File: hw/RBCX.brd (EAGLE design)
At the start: 100 x 100 mm, 463 parts, among them IC1 AMS1117-3.3, IC10 INA180A4, IC11 INA180A4, IC12 MPU-6050, IC13 STM32F103VCT6, IC2 DRV8833PWP, IC3 INA180A4, IC4 INA180A4, IC5 DRV8833PWP, IC6 INA180A4, IC7 INA180A4, IC8 INA180A4, IC9 INA180A4, P1 M1, P2 M2, P3 M3, P4 M4, Q1 NCE20P45Q, Q10 2N7002, Q2 NCE20P45Q, Q3 2N7002, Q4 2N7002, Q5 2N7002, Q6 2N7002, Q7 2N7002, Q8 2N7002, Q9 2N7002, X1 POWER_IN, X2 POWER_OUT, X3 52559-3092, X4 uUSB, Y1 5032/2P, Y2 3215_2P

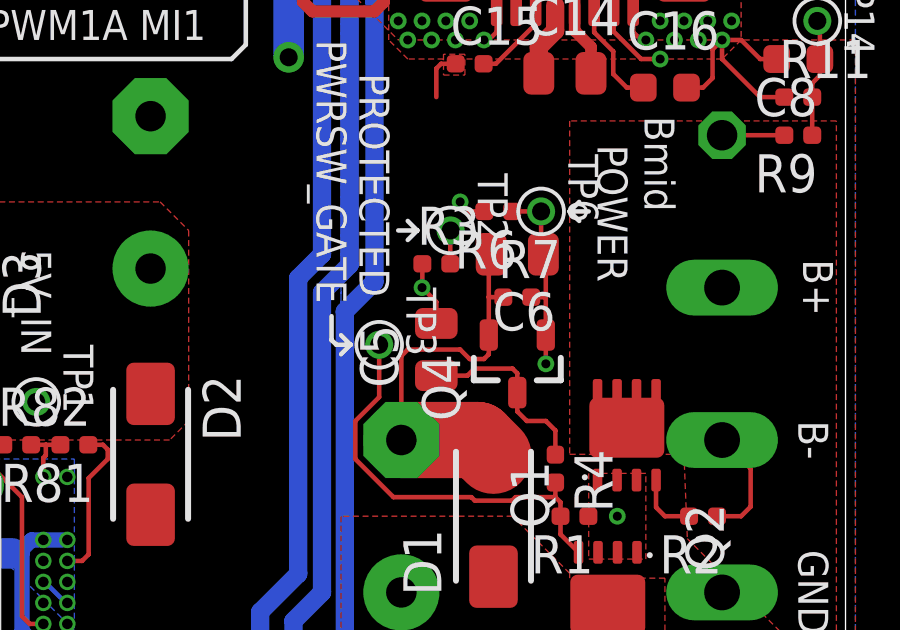
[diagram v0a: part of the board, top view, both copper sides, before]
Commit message: hw: fix power circuit capacitors value
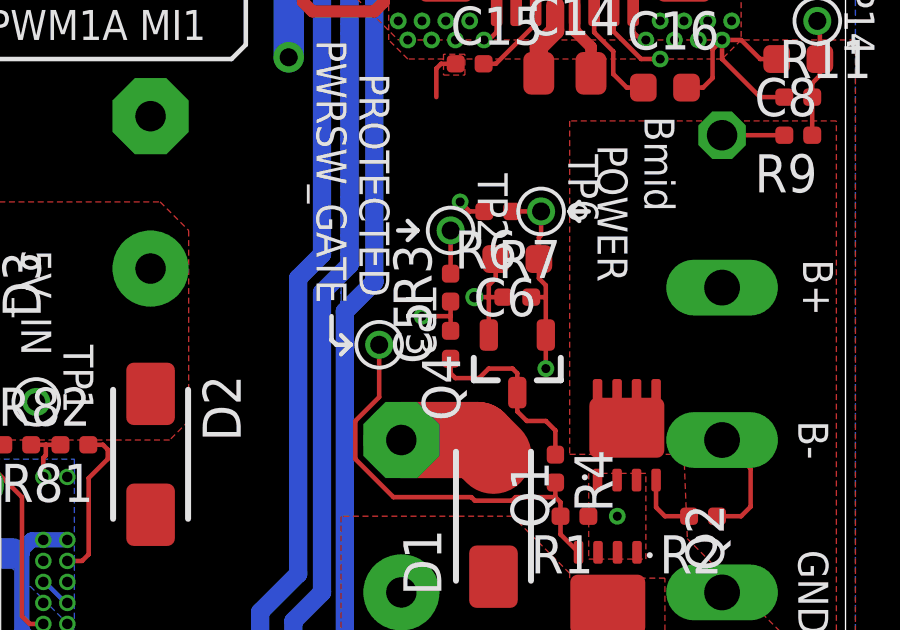
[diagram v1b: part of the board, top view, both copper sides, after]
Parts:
- C5: value 10u -> 100n; device rcl_upravena:C0805 -> rcl_upravena:C0402
- C6: value 10u -> 2u2; device rcl_upravena:C0805 -> rcl_upravena:C0603
- moved R3 0.93 mm to (86.8, 57.8), turned to 90 degrees
- moved C5 0.50 mm to (86.8, 55.9)
- moved C6 0.16 mm to (89.1, 58.7)
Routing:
- net GND: track 636.3 -> 630.1 mm, vias 141 -> 142
- net BUTTON-ON: track 157.5 -> 156.8 mm

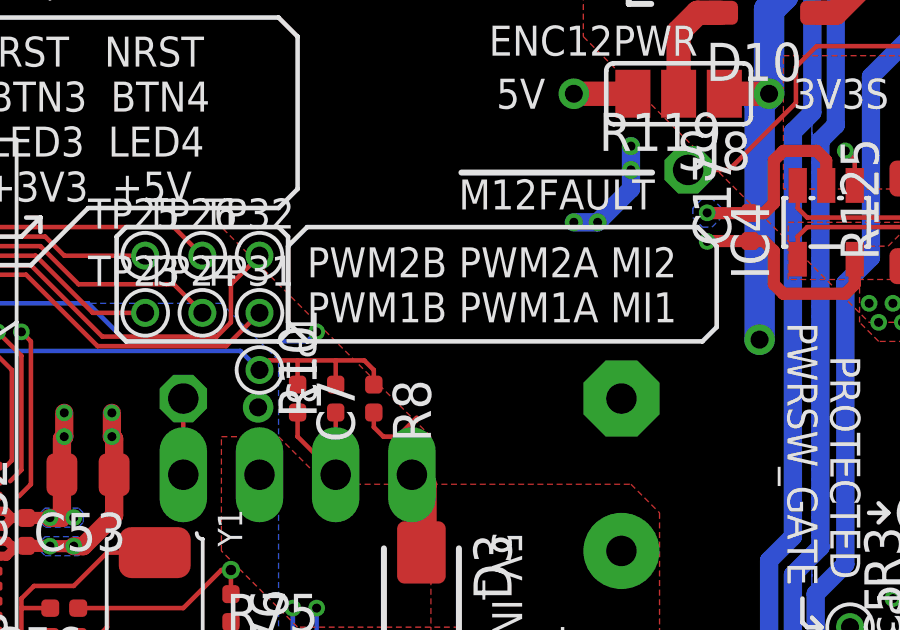
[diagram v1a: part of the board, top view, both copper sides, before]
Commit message: hw: fix power button function without battery connected (only in schematic)
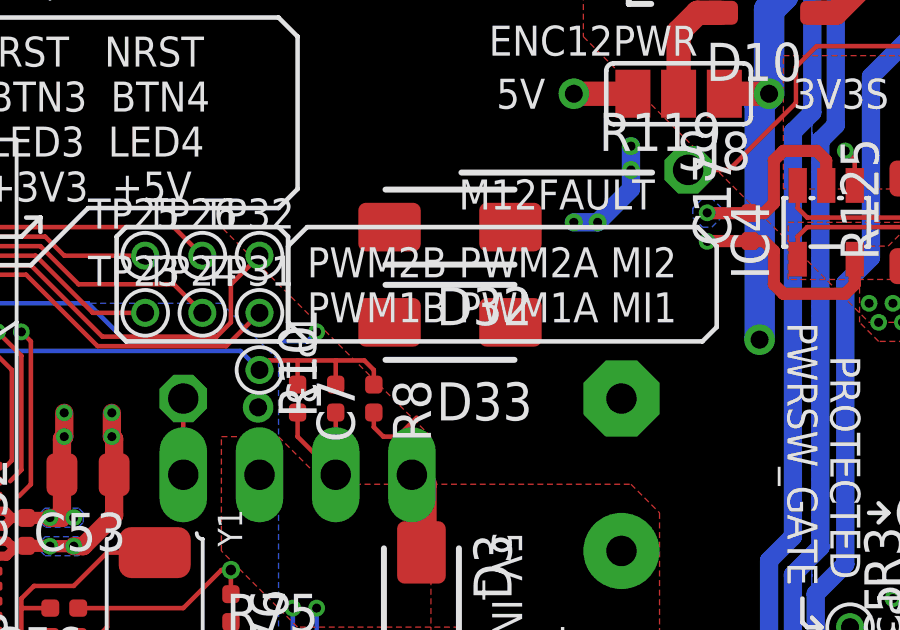
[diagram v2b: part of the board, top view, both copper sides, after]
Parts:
- added D32, D33: SS34, diode:SMA
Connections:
- net +5V: now also D32.A
- net BAT+_PROTECTED: now also D32.C, D33.C
- net VUSB: now also D33.A
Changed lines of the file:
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@@
 <attribute name="VOLTAGE" value="16V" x="89.05875" y="58.7375" size="1.778" layer="27" rot="R180" display="off"/>
 </element>
+<element name="D32" library="diode" package="SMA" value="SS34" x="71.12" y="69.215" smashed="yes" rot="R180">
+<attribute name="NAME" x="73.87" y="67.215" size="1.27" layer="25" ratio="10" rot="R180"/>
+<attribute name="VALUE" x="73.87" y="72.715" size="1.27" layer="27" ratio="10" rot="R180"/>
+</element>
+<element name="D33" library="diode" package="SMA" value="SS34" x="71.12" y="66.04" smashed="yes" rot="R180">
+<attribute name="NAME" x="73.87" y="64.04" size="1.27" layer="25" ratio="10" rot="R180"/>
+<attribute name="VALUE" x="73.87" y="69.54" size="1.27" layer="27" ratio="10" rot="R180"/>
+</element>
 </elements>
 <signals>
@@
 <wire x1="92.3925" y1="54.13375" x2="86.83625" y2="59.69" width="0.6096" layer="2"/>
 <wire x1="86.83625" y1="58.25" x2="86.83625" y2="59.69" width="0.1524" layer="1"/>
+<contactref element="D32" pad="C"/>
+<contactref element="D33" pad="C"/>
 <wire x1="92.385" y1="51.36875" x2="91.735" y2="51.36875" width="0" layer="19" extent="1-1"/>
 <wire x1="93.035" y1="51.36875" x2="92.385" y2="51.36875" width="0" layer="19" extent="1-1"/>
@@
 <wire x1="91.75" y1="48.96125" x2="92.4" y2="48.96125" width="0" layer="19" extent="1-1"/>
 <wire x1="93.05" y1="48.96125" x2="92.4" y2="48.96125" width="0" layer="19" extent="1-1"/>
+<wire x1="73.135" y1="69.215" x2="91.75" y2="48.96125" width="0" layer="19" extent="1-1"/>
+<wire x1="73.135" y1="66.04" x2="73.135" y2="69.215" width="0" layer="19" extent="1-1"/>
 </signal>
 <signal name="BAT+">
@@
 <wire x1="33.655" y1="6.604" x2="33.655" y2="6.59375" width="0.1524" layer="1"/>
 <wire x1="8.9535" y1="10.16" x2="8.96375" y2="10.16" width="0.1524" layer="1"/>
+<contactref element="D32" pad="A"/>
+<wire x1="76.835" y1="95.885" x2="76.835" y2="98.425" width="0" layer="19" extent="1-1"/>
+<wire x1="76.835" y1="93.345" x2="76.835" y2="95.885" width="0" layer="19" extent="1-1"/>
+<wire x1="76.835" y1="90.805" x2="76.835" y2="93.345" width="0" layer="19" extent="1-1"/>
+<wire x1="76.835" y1="86.36" x2="77.355" y2="87.78875" width="0" layer="19" extent="1-1"/>
+<wire x1="67.6275" y1="83.02625" x2="76.835" y2="86.36" width="0" layer="19" extent="1-1"/>
+<wire x1="66.04" y1="83.02625" x2="67.6275" y2="83.02625" width="0" layer="19" extent="1-1"/>
+<wire x1="66.04" y1="81.43875" x2="66.04" y2="83.02625" width="0" layer="19" extent="1-1"/>
+<wire x1="67.6275" y1="81.43875" x2="67.6275" y2="83.02625" width="0" layer="19" extent="1-1"/>
+<wire x1="64.325" y1="82.2325" x2="66.04" y2="83.02625" width="0" layer="19" extent="1-1"/>
+<wire x1="75.2475" y1="73.66" x2="67.6275" y2="81.43875" width="0" layer="19" extent="1-1"/>
+<wire x1="69.85" y1="60.96" x2="75.2475" y2="73.66" width="0" layer="19" extent="1-1"/>
+<wire x1="65.515" y1="33.3375" x2="70.1675" y2="58.37125" width="0" layer="19" extent="1-1"/>
+<wire x1="81.5975" y1="29.845" x2="69.5325" y2="30.7975" width="0" layer="19" extent="1-1"/>
+<wire x1="81.915" y1="8.89" x2="81.661" y2="27.94" width="0" layer="19" extent="1-1"/>
+<wire x1="81.915" y1="6.35" x2="81.915" y2="8.89" width="0" layer="19" extent="1-1"/>
+<wire x1="81.915" y1="3.81" x2="81.915" y2="6.35" width="0" layer="19" extent="1-1"/>
+<wire x1="81.915" y1="1.27" x2="81.915" y2="3.81" width="0" layer="19" extent="1-1"/>
+<wire x1="53.975" y1="8.255" x2="69.5325" y2="30.7975" width="0" layer="19" extent="1-1"/>
+<wire x1="33.655" y1="8.09625" x2="53.975" y2="8.255" width="0" layer="19" extent="1-1"/>
+<wire x1="8.9535" y1="6.35" x2="33.655" y2="6.604" width="0" layer="19" extent="1-1"/>
+<wire x1="69.105" y1="69.215" x2="8.9535" y2="2.54" width="0" layer="19" extent="1-1"/>
+<wire x1="13.335" y1="27.01" x2="8.96375" y2="10.16" width="0" layer="19" extent="1-1"/>
+<wire x1="9.36625" y1="72.39" x2="8.5725" y2="40.64" width="0" layer="19" extent="1-1"/>
+<wire x1="9.36625" y1="74.93" x2="9.36625" y2="72.39" width="0" layer="19" extent="1-1"/>
+<wire x1="17.78" y1="90.17" x2="9.36625" y2="74.93" width="0" layer="19" extent="1-1"/>
+<wire x1="17.78" y1="91.7575" x2="17.78" y2="90.17" width="0" layer="19" extent="1-1"/>
+<wire x1="19.3675" y1="91.7575" x2="17.78" y2="91.7575" width="0" layer="19" extent="1-1"/>
+<wire x1="19.3675" y1="90.17" x2="17.78" y2="90.17" width="0" layer="19" extent="1-1"/>
+<wire x1="18.9225" y1="93.6625" x2="19.3675" y2="91.7575" width="0" layer="19" extent="1-1"/>
+<wire x1="28.8925" y1="73.18375" x2="19.3675" y2="90.17" width="0" layer="19" extent="1-1"/>
 </signal>
 <signal name="ISERVO">
@@
 <wire x1="73.26" y1="45.875" x2="74.06" y2="45.875" width="0.508" layer="2"/>
 <wire x1="74.06" y1="45.875" x2="74.37375" y2="45.56125" width="0.508" layer="2"/>
+<contactref element="D33" pad="A"/>
+<wire x1="69.105" y1="66.04" x2="3.3625" y2="51.835" width="0" layer="19" extent="1-16"/>
 </signal>
 <signal name="USB_ID">

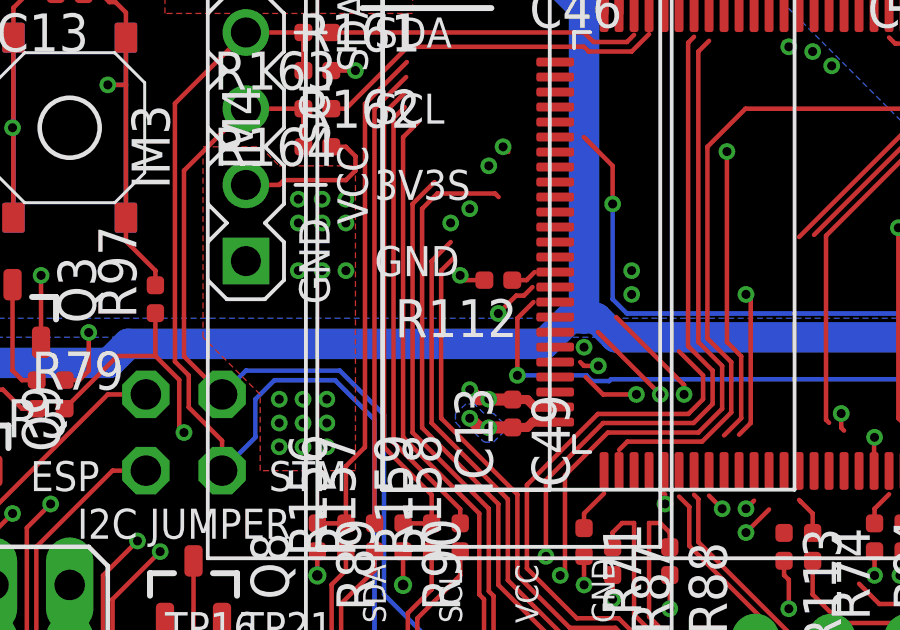
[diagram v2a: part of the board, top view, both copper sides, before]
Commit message: hw: remove resistor between STM and ESP enable
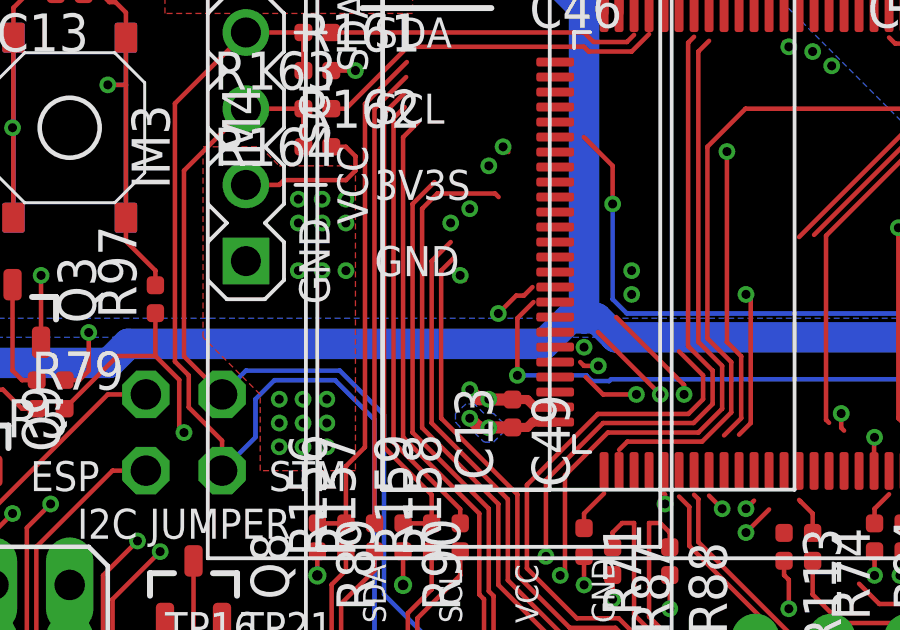
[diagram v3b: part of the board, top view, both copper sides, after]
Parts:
- removed R112: 330R, rcl_upravena:R0402
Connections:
- removed net ESP-EN: IM9.2, JP44.5, R112.2, S13.C, S13.D, S7.C, S7.D, TP60.P$1, X3.15
- net ESP_EN: now also IM9.2, JP44.5, S13.C, S13.D, S7.C, S7.D, TP60.P$1, X3.15; no longer R112.1
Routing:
- net ESP-EN: track 138.8 -> 0.00 mm, vias 4 -> 0
- net ESP_EN: track 0.86 -> 138.2 mm, vias 0 -> 4
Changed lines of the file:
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@@
 <attribute name="VALUE" x="0.47625" y="93.345" size="1.27" layer="28" rot="MR180"/>
 </element>
-<element name="R112" library="rcl_upravena" package="R0402" value="330R" x="38.4175" y="53.975" smashed="yes" rot="R180">
-<attribute name="NAME" x="39.0525" y="53.34" size="1.27" layer="25" rot="R180"/>
-<attribute name="VALUE" x="39.0525" y="55.88" size="1.27" layer="27" rot="R180"/>
-</element>
 <element name="IC12" library="MPU-6050" package="QFN50P400X400X95-24N" value="MPU-6050" x="51.435" y="24.765" smashed="yes" rot="R270">
 <attribute name="AVAILABILITY" value="Unavailable" x="51.435" y="24.765" size="1.778" layer="27" rot="R270" display="off"/>
@@
 <wire x1="4.7625" y1="38.25875" x2="6.50875" y2="38.25875" width="0.1524" layer="2"/>
 </signal>
-<signal name="ESP-EN">
-<contactref element="X3" pad="15"/>
-<contactref element="R112" pad="2"/>
-<contactref element="JP44" pad="5"/>
-<contactref element="IM9" pad="2"/>
-<contactref element="S7" pad="C"/>
-<contactref element="S7" pad="D"/>
-<contactref element="TP60" pad="P$1"/>
-<wire x1="6.16125" y1="8.90625" x2="6.16125" y2="14.90625" width="0.1524" layer="1"/>
-<wire x1="37.1475" y1="54.13375" x2="37.30625" y2="53.975" width="0.1524" layer="1"/>
-<wire x1="37.9525" y1="53.975" x2="37.30625" y2="53.975" width="0.1524" layer="1"/>
-<via x="37.1475" y="54.13375" extent="1-16" drill="0.3"/>
-<via x="9.2075" y="56.99125" extent="1-16" drill="0.3"/>
-<wire x1="9.2075" y1="56.99125" x2="8.89" y2="56.67375" width="0.1524" layer="1"/>
-<wire x1="8.89" y1="56.67375" x2="8.89" y2="44.45" width="0.1524" layer="1"/>
-<wire x1="5.715" y1="44.45" x2="8.89" y2="44.45" width="0.1524" layer="1"/>
-<wire x1="11.43" y1="38.1" x2="11.4276" y2="38.1024" width="0.1524" layer="1"/>
-<wire x1="11.4276" y1="38.1024" x2="11.4276" y2="39.6320375" width="0.1524" layer="1"/>
-<wire x1="8.89" y1="42.1696375" x2="8.89" y2="44.45" width="0.1524" layer="1"/>
-<wire x1="11.4276" y1="39.6320375" x2="8.89" y2="42.1696375" width="0.1524" layer="1"/>
-<wire x1="9.2075" y1="56.99125" x2="9.2075" y2="62.5475" width="0.1524" layer="1"/>
-<wire x1="7.9375" y1="89.05875" x2="6.82625" y2="90.17" width="0.1524" layer="1"/>
-<wire x1="9.2075" y1="56.99125" x2="27.14625" y2="56.99125" width="0.1524" layer="2"/>
-<wire x1="27.14625" y1="56.99125" x2="28.41625" y2="55.72125" width="0.1524" layer="2"/>
-<wire x1="28.41625" y1="55.72125" x2="30.63875" y2="55.72125" width="0.1524" layer="2"/>
-<wire x1="36.35375" y1="54.9275" x2="37.1475" y2="54.13375" width="0.1524" layer="2"/>
-<wire x1="36.35375" y1="54.9275" x2="31.4325" y2="54.9275" width="0.1524" layer="2"/>
-<wire x1="31.4325" y1="54.9275" x2="30.63875" y2="55.72125" width="0.1524" layer="2"/>
-<wire x1="3.3625" y1="44.835" x2="4.3775" y2="44.835" width="0.1524" layer="16"/>
-<wire x1="4.445" y1="44.7675" x2="4.3775" y2="44.835" width="0.1524" layer="16"/>
-<wire x1="4.445" y1="44.7675" x2="4.7625" y2="44.7675" width="0.1524" layer="16"/>
-<via x="4.7625" y="44.7675" extent="1-16" drill="0.3"/>
-<wire x1="4.7625" y1="44.7675" x2="5.3975" y2="44.7675" width="0.1524" layer="1"/>
-<wire x1="5.3975" y1="44.7675" x2="5.715" y2="44.45" width="0.1524" layer="1"/>
-<wire x1="9.2075" y1="62.5475" x2="10.795" y2="64.135" width="0.1524" layer="1"/>
-<wire x1="10.795" y1="64.135" x2="10.795" y2="88.265" width="0.1524" layer="1"/>
-<wire x1="10.00125" y1="89.05875" x2="7.9375" y2="89.05875" width="0.1524" layer="1"/>
-<wire x1="10.795" y1="88.265" x2="10.00125" y2="89.05875" width="0.1524" layer="1"/>
-<wire x1="9.36625" y1="92.71" x2="6.82625" y2="90.17" width="0.1524" layer="2"/>
-<wire x1="7.77875" y1="39.0525" x2="7.18185" y2="38.4556" width="0.1524" layer="2"/>
-<wire x1="10.4775" y1="39.0525" x2="11.43" y2="38.1" width="0.1524" layer="2"/>
-<wire x1="7.77875" y1="39.0525" x2="10.4775" y2="39.0525" width="0.1524" layer="2"/>
-<wire x1="7.18185" y1="16.70685" x2="6.985" y2="16.51" width="0.1524" layer="2"/>
-<via x="6.985" y="16.51" extent="1-16" drill="0.3"/>
-<wire x1="6.985" y1="16.51" x2="6.16125" y2="15.68625" width="0.1524" layer="1"/>
-<wire x1="6.16125" y1="15.68625" x2="6.16125" y2="14.90625" width="0.1524" layer="1"/>
-<wire x1="7.18185" y1="38.4556" x2="7.18185" y2="16.70685" width="0.1524" layer="2"/>
-<contactref element="S13" pad="C"/>
-<contactref element="S13" pad="D"/>
-<wire x1="6.16125" y1="8.90625" x2="6.16125" y2="14.90625" width="0.1524" layer="16"/>
-<wire x1="6.16125" y1="14.90625" x2="6.16125" y2="15.68625" width="0.1524" layer="16"/>
-<wire x1="6.16125" y1="15.68625" x2="6.985" y2="16.51" width="0.1524" layer="16"/>
-</signal>
 <signal name="PWRSW_GATE">
 <contactref element="R1" pad="2"/>
@@
 </signal>
 <signal name="ESP_EN">
-<contactref element="R112" pad="1"/>
-<wire x1="38.8825" y1="53.975" x2="39.35875" y2="53.975" width="0.1524" layer="1"/>
-<wire x1="39.62875" y1="54.245" x2="39.35875" y2="53.975" width="0.1524" layer="1"/>
 <contactref element="IC13" pad="85"/>
-<wire x1="46.4425" y1="47.615" x2="39.62875" y2="54.245" width="0" layer="19" extent="1-1"/>
+<contactref element="X3" pad="15"/>
+<contactref element="JP44" pad="5"/>
+<contactref element="IM9" pad="2"/>
+<contactref element="S7" pad="C"/>
+<contactref element="S7" pad="D"/>
+<contactref element="TP60" pad="P$1"/>
+<wire x1="6.16125" y1="8.90625" x2="6.16125" y2="14.90625" width="0.1524" layer="1"/>
+<wire x1="37.1475" y1="54.13375" x2="37.30625" y2="53.975" width="0.1524" layer="1"/>
+<via x="37.1475" y="54.13375" extent="1-16" drill="0.3"/>
+<via x="9.2075" y="56.99125" extent="1-16" drill="0.3"/>
+<wire x1="9.2075" y1="56.99125" x2="8.89" y2="56.67375" width="0.1524" layer="1"/>
+<wire x1="8.89" y1="56.67375" x2="8.89" y2="44.45" width="0.1524" layer="1"/>
+<wire x1="5.715" y1="44.45" x2="8.89" y2="44.45" width="0.1524" layer="1"/>
+<wire x1="11.43" y1="38.1" x2="11.4276" y2="38.1024" width="0.1524" layer="1"/>
+<wire x1="11.4276" y1="38.1024" x2="11.4276" y2="39.6320375" width="0.1524" layer="1"/>
+<wire x1="8.89" y1="42.1696375" x2="8.89" y2="44.45" width="0.1524" layer="1"/>
+<wire x1="11.4276" y1="39.6320375" x2="8.89" y2="42.1696375" width="0.1524" layer="1"/>
+<wire x1="9.2075" y1="56.99125" x2="9.2075" y2="62.5475" width="0.1524" layer="1"/>
+<wire x1="7.9375" y1="89.05875" x2="6.82625" y2="90.17" width="0.1524" layer="1"/>
+<wire x1="9.2075" y1="56.99125" x2="27.14625" y2="56.99125" width="0.1524" layer="2"/>
+<wire x1="27.14625" y1="56.99125" x2="28.41625" y2="55.72125" width="0.1524" layer="2"/>
+<wire x1="28.41625" y1="55.72125" x2="30.63875" y2="55.72125" width="0.1524" layer="2"/>
+<wire x1="36.35375" y1="54.9275" x2="37.1475" y2="54.13375" width="0.1524" layer="2"/>
+<wire x1="36.35375" y1="54.9275" x2="31.4325" y2="54.9275" width="0.1524" layer="2"/>
+<wire x1="31.4325" y1="54.9275" x2="30.63875" y2="55.72125" width="0.1524" layer="2"/>
+<wire x1="3.3625" y1="44.835" x2="4.3775" y2="44.835" width="0.1524" layer="16"/>
+<wire x1="4.445" y1="44.7675" x2="4.3775" y2="44.835" width="0.1524" layer="16"/>
+<wire x1="4.445" y1="44.7675" x2="4.7625" y2="44.7675" width="0.1524" layer="16"/>
+<via x="4.7625" y="44.7675" extent="1-16" drill="0.3"/>
+<wire x1="4.7625" y1="44.7675" x2="5.3975" y2="44.7675" width="0.1524" layer="1"/>
+<wire x1="5.3975" y1="44.7675" x2="5.715" y2="44.45" width="0.1524" layer="1"/>
+<wire x1="9.2075" y1="62.5475" x2="10.795" y2="64.135" width="0.1524" layer="1"/>
+<wire x1="10.795" y1="64.135" x2="10.795" y2="88.265" width="0.1524" layer="1"/>
+<wire x1="10.00125" y1="89.05875" x2="7.9375" y2="89.05875" width="0.1524" layer="1"/>
+<wire x1="10.795" y1="88.265" x2="10.00125" y2="89.05875" width="0.1524" layer="1"/>
+<wire x1="9.36625" y1="92.71" x2="6.82625" y2="90.17" width="0.1524" layer="2"/>
+<wire x1="7.77875" y1="39.0525" x2="7.18185" y2="38.4556" width="0.1524" layer="2"/>
+<wire x1="10.4775" y1="39.0525" x2="11.43" y2="38.1" width="0.1524" layer="2"/>
+<wire x1="7.77875" y1="39.0525" x2="10.4775" y2="39.0525" width="0.1524" layer="2"/>
+<wire x1="7.18185" y1="16.70685" x2="6.985" y2="16.51" width="0.1524" layer="2"/>
+<via x="6.985" y="16.51" extent="1-16" drill="0.3"/>
+<wire x1="6.985" y1="16.51" x2="6.16125" y2="15.68625" width="0.1524" layer="1"/>
+<wire x1="6.16125" y1="15.68625" x2="6.16125" y2="14.90625" width="0.1524" layer="1"/>
+<wire x1="7.18185" y1="38.4556" x2="7.18185" y2="16.70685" width="0.1524" layer="2"/>
+<contactref element="S13" pad="C"/>
+<contactref element="S13" pad="D"/>
+<wire x1="6.16125" y1="8.90625" x2="6.16125" y2="14.90625" width="0.1524" layer="16"/>
+<wire x1="6.16125" y1="14.90625" x2="6.16125" y2="15.68625" width="0.1524" layer="16"/>
+<wire x1="6.16125" y1="15.68625" x2="6.985" y2="16.51" width="0.1524" layer="16"/>
+<wire x1="37.30625" y1="53.975" x2="46.4425" y2="47.615" width="0" layer="19" extent="1-1"/>
 </signal>
 <signal name="STM-I2C-SDA">
